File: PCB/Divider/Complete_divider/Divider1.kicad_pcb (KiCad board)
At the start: 2 copper layers, 103.8 x 48 mm, 56 parts, among them J1 10kV

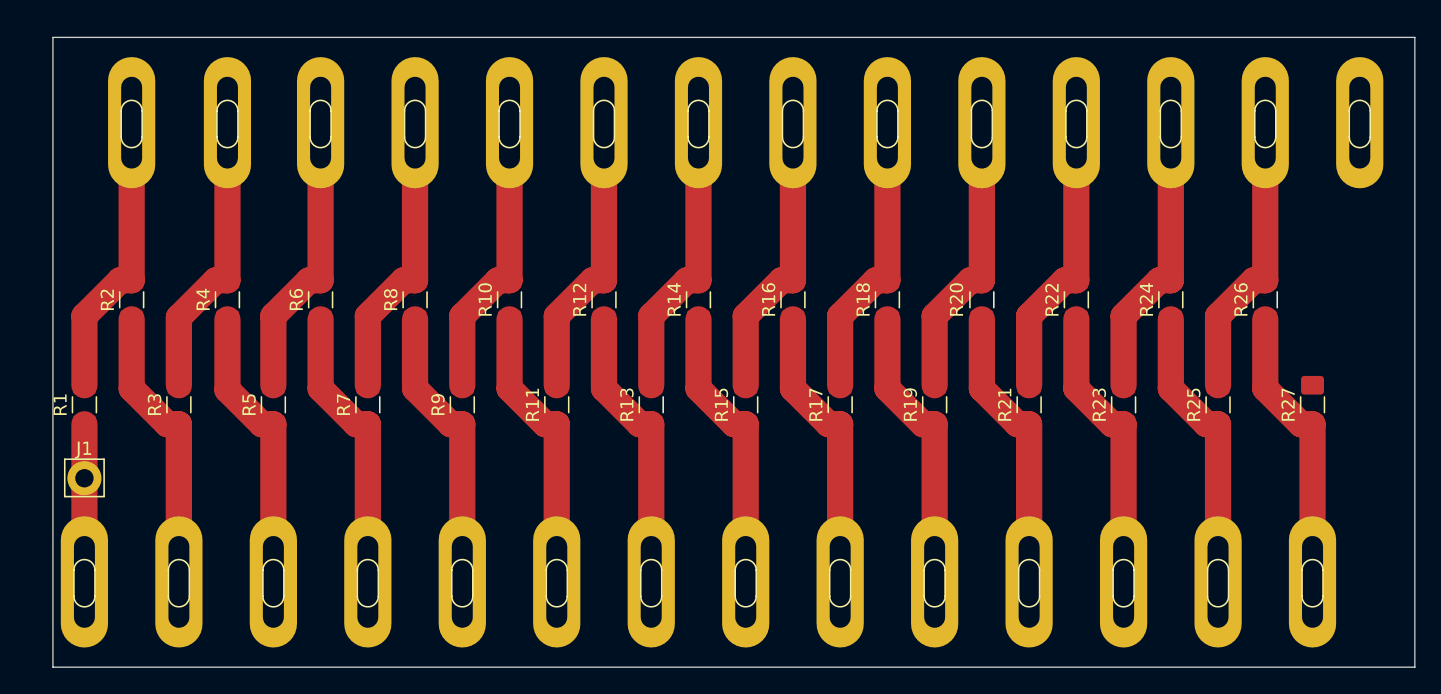
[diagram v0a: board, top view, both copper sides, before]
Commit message: Dividers finished without testing points
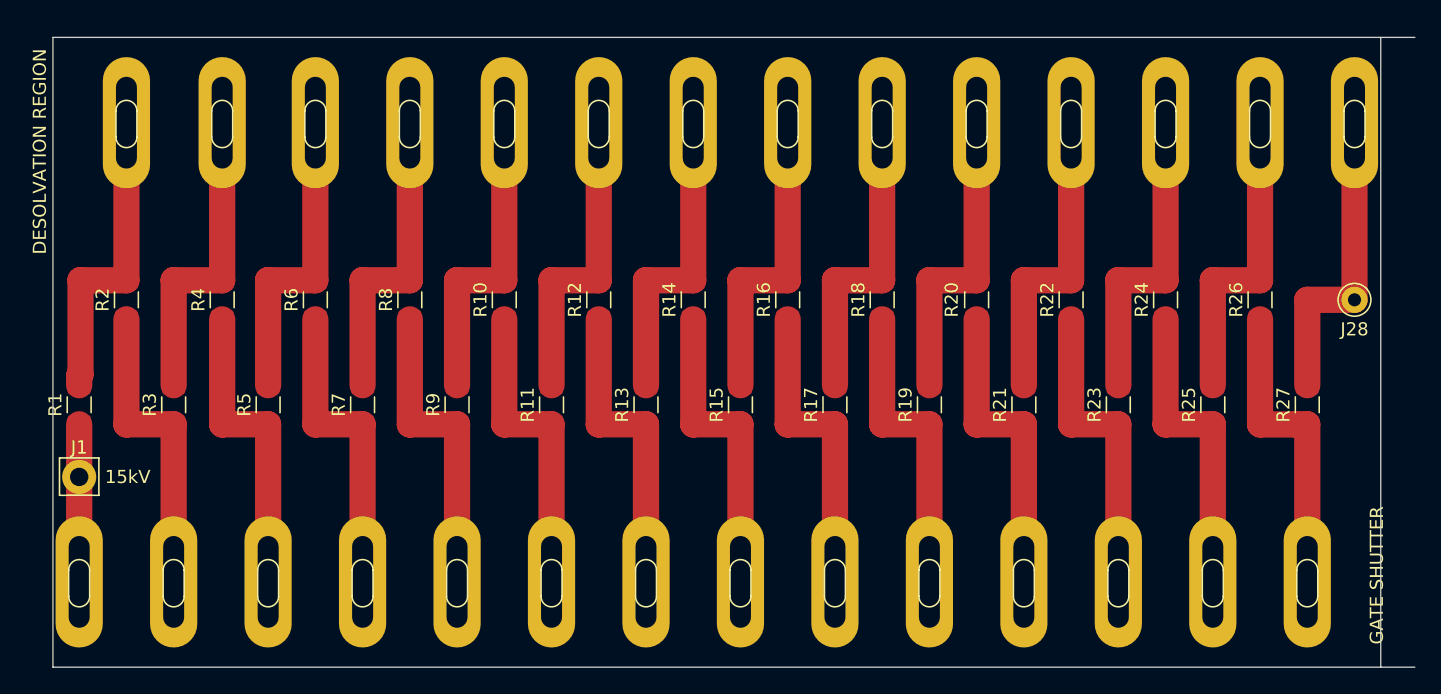
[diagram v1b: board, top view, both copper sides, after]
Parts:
- added J28: Electr., Connector_Pin:Pin_D1.0mm_L10.0mm, F.Cu at (148.2, 72.0)
- moved J1 0.41 mm to (51.0, 85.5)
- moved E11 0.40 mm to (87.0, 93.6)
- moved E12 0.40 mm to (90.6, 58.6)
- moved E14 0.40 mm to (97.8, 58.6)
- moved E16 0.40 mm to (105.0, 58.6)
- moved E17 0.40 mm to (108.6, 93.6)
- moved E19 0.40 mm to (115.8, 93.6)
- moved E21 0.40 mm to (123.0, 93.6)
- moved E22 0.40 mm to (126.6, 58.6)
- moved E23 0.40 mm to (130.2, 93.6)
- moved E25 0.40 mm to (137.4, 93.6)
- moved E26 0.40 mm to (141.0, 58.6)
- moved E27 0.40 mm to (144.6, 93.6)
- moved E28 0.40 mm to (148.2, 58.6)
- moved E6 0.40 mm to (69.0, 58.6)
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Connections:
- net DRIFTTUBE renamed DESOLVATION
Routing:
- net TRI-STATE: track 0.00 -> 23.6 mm
- net Net-(E4-Pad1): track 22.1 -> 23.7 mm
- net Net-(E24-Pad1): track 22.0 -> 23.6 mm
- net Net-(E8-Pad1): track 22.0 -> 23.6 mm
- net Net-(E20-Pad1): track 22.0 -> 23.6 mm
- net Net-(E18-Pad1): track 22.0 -> 23.6 mm
- net Net-(E15-Pad1): track 22.0 -> 23.6 mm
- net Net-(E13-Pad1): track 22.0 -> 23.6 mm
- net Net-(E10-Pad1): track 22.0 -> 23.6 mm
- net Net-(E3-Pad1): track 22.0 -> 23.6 mm
- net Net-(E27-Pad1): track 22.0 -> 23.6 mm
- net Net-(E26-Pad1): track 22.0 -> 23.6 mm
- net Net-(E7-Pad1): track 22.0 -> 23.6 mm
- net Net-(E23-Pad1): track 22.0 -> 23.6 mm
- net Net-(E22-Pad1): track 22.0 -> 23.6 mm
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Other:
- outline, holes or cut-outs redrawn
- board text added: "15kV"
- board text added: "DESOLVATION REGION"
- board text added: "GATE SHUTTER"

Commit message: Divider finished with test points
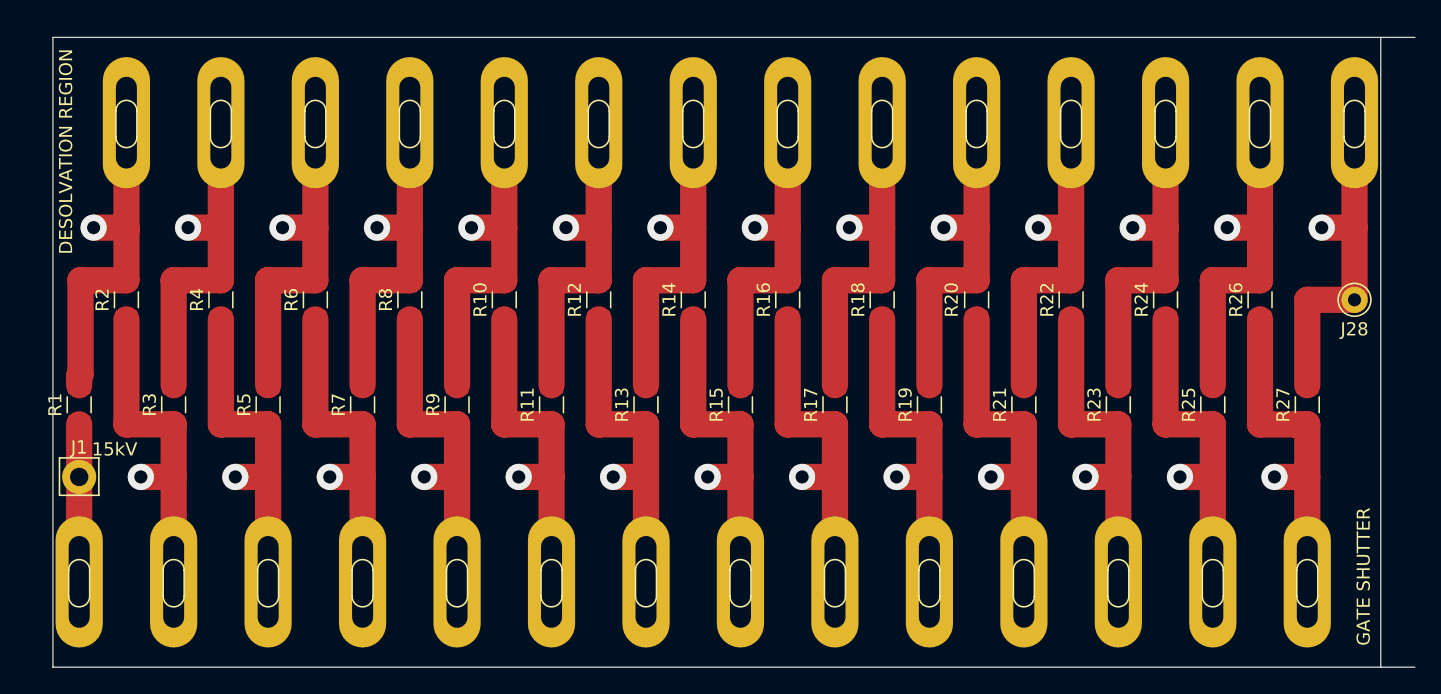
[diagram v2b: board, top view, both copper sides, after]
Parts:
- moved E4 0.10 mm to (61.8, 58.6)
- moved R4 0.10 mm to (61.8, 72.0)
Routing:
- net Net-(E5-Pad1): track 23.5 -> 26.1 mm, vias 0 -> 1
- net Net-(E24-Pad1): track 23.6 -> 26.1 mm, vias 0 -> 1
- net Net-(E2-Pad1): track 23.6 -> 26.1 mm, vias 0 -> 1
- net TRI-STATE: track 23.6 -> 26.1 mm, vias 0 -> 1
- net Net-(E9-Pad1): track 23.6 -> 26.1 mm, vias 0 -> 1
- net Net-(E8-Pad1): track 23.6 -> 26.1 mm, vias 0 -> 1
- net Net-(E7-Pad1): track 23.6 -> 26.1 mm, vias 0 -> 1
- net Net-(E6-Pad1): track 23.6 -> 26.1 mm, vias 0 -> 1
- net Net-(E3-Pad1): track 23.6 -> 26.1 mm, vias 0 -> 1
- net Net-(E27-Pad1): track 23.6 -> 26.1 mm, vias 0 -> 1
- net Net-(E26-Pad1): track 23.6 -> 26.1 mm, vias 0 -> 1
- net Net-(E25-Pad1): track 23.6 -> 26.1 mm, vias 0 -> 1
- net Net-(E22-Pad1): track 23.6 -> 26.1 mm, vias 0 -> 1
- net Net-(E21-Pad1): track 23.6 -> 26.1 mm, vias 0 -> 1
- net Net-(E20-Pad1): track 23.6 -> 26.1 mm, vias 0 -> 1
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
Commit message: Updates of dividers 1 & 2
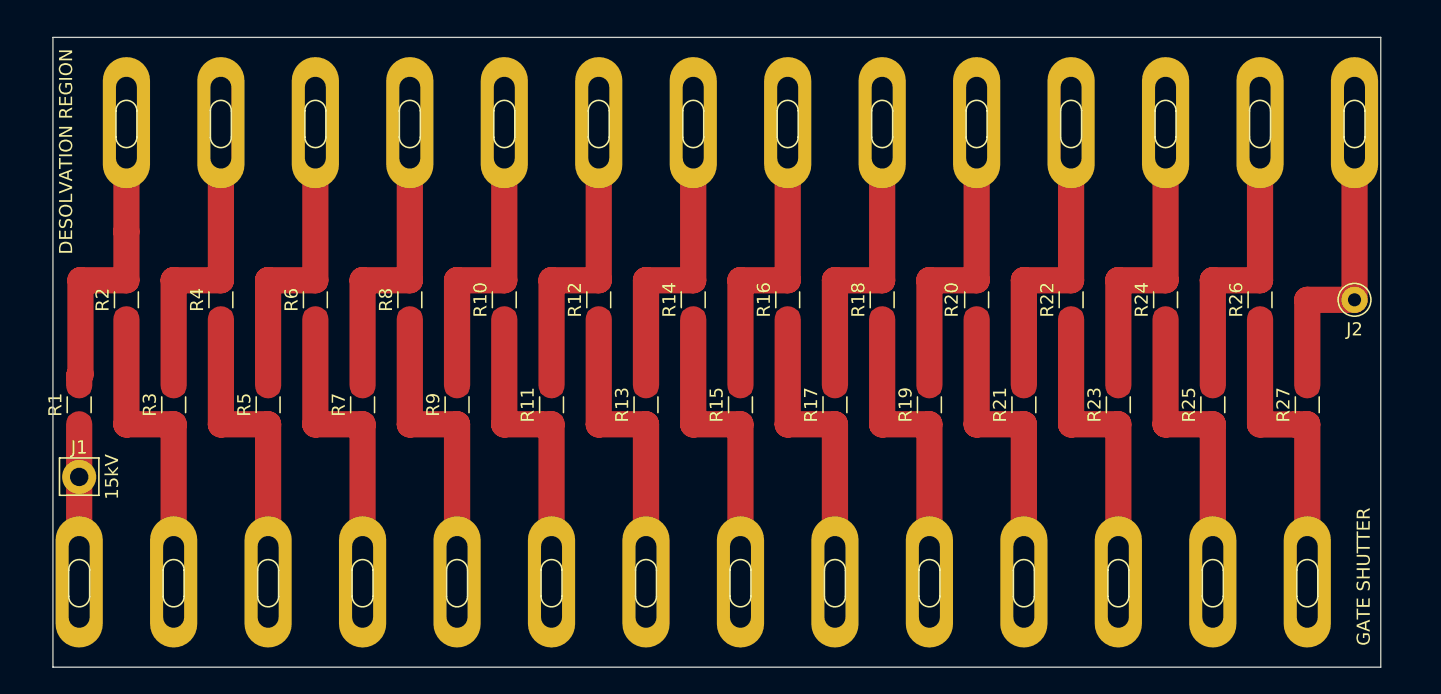
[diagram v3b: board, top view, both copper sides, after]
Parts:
- J1: value 10kV -> 15kV
- renumbered J28 to J2
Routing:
- net Net-(E5-Pad1): track 26.1 -> 23.6 mm, vias 1 -> 0
- net Net-(E24-Pad1): track 26.1 -> 23.6 mm, vias 1 -> 0
- net TRI-STATE: track 26.1 -> 23.6 mm, vias 1 -> 0
- net Net-(E9-Pad1): track 26.1 -> 23.6 mm, vias 1 -> 0
- net Net-(E8-Pad1): track 26.1 -> 23.6 mm, vias 1 -> 0
- net Net-(E7-Pad1): track 26.1 -> 23.6 mm, vias 1 -> 0
- net Net-(E6-Pad1): track 26.1 -> 23.6 mm, vias 1 -> 0
- net Net-(E4-Pad1): track 26.1 -> 23.6 mm, vias 1 -> 0
- net Net-(E3-Pad1): track 26.1 -> 23.6 mm, vias 1 -> 0
- net Net-(E27-Pad1): track 26.1 -> 23.6 mm, vias 1 -> 0
- net Net-(E26-Pad1): track 26.1 -> 23.6 mm, vias 1 -> 0
- net Net-(E25-Pad1): track 26.1 -> 23.6 mm, vias 1 -> 0
- net Net-(E22-Pad1): track 26.1 -> 23.6 mm, vias 1 -> 0
- net Net-(E21-Pad1): track 26.1 -> 23.6 mm, vias 1 -> 0
- net Net-(E20-Pad1): track 26.1 -> 23.6 mm, vias 1 -> 0
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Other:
- board size 103.8 x 48 mm -> 101.2 x 48 mm
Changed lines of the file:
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@@
     (thickness 1.6)
     (drawings 15)
-    (tracks 195)
+    (tracks 114)
     (zones 0)
     (modules 57)
@@
     (descr "solder Pin_ diameter 1.0mm, hole diameter 1.0mm (press fit), length 10.0mm")
     (tags "solder Pin_ press fit")
-    (fp_text reference J28 (at 0 2.25) (layer F.SilkS)
+    (fp_text reference J2 (at 0 2.25) (layer F.SilkS)
       (effects (font (size 1 1) (thickness 0.15)))
     )
@@
       (effects (font (size 1 1) (thickness 0.15)))
     )
-    (fp_text value 10kV (at 0 -2.05) (layer F.Fab)
+    (fp_text value 15kV (at 0 -2.05) (layer F.Fab)
       (effects (font (size 1 1) (thickness 0.15)))
     )
@@
     )
   )
+  (gr_line (start 49 100) (end 150.2 100) (layer Edge.Cuts) (width 0.05))
   (gr_text "GATE SHUTTER" (at 148.9 93.1 90) (layer F.SilkS)
     (effects (font (size 1 1) (thickness 0.15)))
@@
     (effects (font (size 1 1) (thickness 0.15)))
   )
-  (gr_text "15kV\n" (at 53.7 83.4) (layer F.SilkS)
+  (gr_text "15kV\n" (at 53.5 85.5 90) (layer F.SilkS)
     (effects (font (size 1 1) (thickness 0.15)))
   )
@@
   (gr_line (start 44.2 93.5) (end 150.6 93.5) (layer Dwgs.User) (width 0.15))
   (gr_line (start 150.2 100) (end 150.2 52) (layer Edge.Cuts) (width 0.05))
-  (gr_line (start 49 100) (end 152.8 100) (layer Edge.Cuts) (width 0.05))
   (gr_line (start 49 52) (end 49 100) (layer Edge.Cuts) (width 0.05))
   (dimension 101.2 (width 0.15) (layer Dwgs.User)
@@
     (arrow2b (pts (xy 29.434179 52.129268) (xy 30.035768 53.247745)))
   )
-  (gr_line (start 152.8 52) (end 49 52) (layer Edge.Cuts) (width 0.05))
+  (gr_line (start 150.2 52) (end 49 52) (layer Edge.Cuts) (width 0.05))
   (segment (start 51.1125 70.5125) (end 54.6 70.5125) (width 2) (layer F.Cu) (net 1))
   (segment (start 51.1 70.5) (end 51.1125 70.5125) (width 2) (layer F.Cu) (net 1))
@@
   (segment (start 54.6 70.5125) (end 54.6 66.8) (width 2) (layer F.Cu) (net 1))
   (segment (start 54.6 66.8) (end 54.6 58.5) (width 2) (layer F.Cu) (net 1))
-  (segment (start 54.6 66.5) (end 52.1 66.5) (width 2) (layer F.Cu) (net 1))
-  (segment (start 52.1 66.5) (end 52.1 66.5) (width 2) (layer F.Cu) (net 1))
-  (via (at 52.1 66.5) (size 2) (drill 1) (layers F.Cu B.Cu) (net 1))
-  (via (at 59.3 66.5) (size 2) (drill 1) (layers F.Cu B.Cu) (net 3))
-  (via (at 66.5 66.5) (size 2) (drill 1) (layers F.Cu B.Cu) (net 5))
-  (via (at 73.7 66.5) (size 2) (drill 1) (layers F.Cu B.Cu) (net 7))
-  (via (at 80.9 66.5) (size 2) (drill 1) (layers F.Cu B.Cu) (net 9))
-  (via (at 88.1 66.5) (size 2) (drill 1) (layers F.Cu B.Cu) (net 11))
-  (via (at 95.3 66.5) (size 2) (drill 1) (layers F.Cu B.Cu) (net 13))
-  (via (at 102.5 66.5) (size 2) (drill 1) (layers F.Cu B.Cu) (net 14))
-  (via (at 109.7 66.5) (size 2) (drill 1) (layers F.Cu B.Cu) (net 16))
-  (via (at 116.9 66.5) (size 2) (drill 1) (layers F.Cu B.Cu) (net 18))
-  (via (at 124.1 66.5) (size 2) (drill 1) (layers F.Cu B.Cu) (net 20))
-  (via (at 131.3 66.5) (size 2) (drill 1) (layers F.Cu B.Cu) (net 22))
-  (via (at 138.5 66.5) (size 2) (drill 1) (layers F.Cu B.Cu) (net 24))
-  (via (at 145.7 66.5) (size 2) (drill 1) (layers F.Cu B.Cu) (net 26))
-  (via (at 55.7 85.5) (size 2) (drill 1) (layers F.Cu B.Cu) (net 2))
-  (via (at 62.9 85.5) (size 2) (drill 1) (layers F.Cu B.Cu) (net 4))
-  (via (at 70.1 85.5) (size 2) (drill 1) (layers F.Cu B.Cu) (net 6))
-  (via (at 77.3 85.5) (size 2) (drill 1) (layers F.Cu B.Cu) (net 8))
-  (via (at 84.5 85.5) (size 2) (drill 1) (layers F.Cu B.Cu) (net 10))
-  (via (at 91.7 85.5) (size 2) (drill 1) (layers F.Cu B.Cu) (net 12))
-  (via (at 98.9 85.5) (size 2) (drill 1) (layers F.Cu B.Cu) (net 27))
-  (via (at 106.1 85.5) (size 2) (drill 1) (layers F.Cu B.Cu) (net 15))
-  (via (at 113.3 85.5) (size 2) (drill 1) (layers F.Cu B.Cu) (net 17))
-  (via (at 120.5 85.5) (size 2) (drill 1) (layers F.Cu B.Cu) (net 19))
-  (via (at 127.7 85.5) (size 2) (drill 1) (layers F.Cu B.Cu) (net 21))
-  (via (at 134.9 85.5) (size 2) (drill 1) (layers F.Cu B.Cu) (net 23))
-  (via (at 142.1 85.5) (size 2) (drill 1) (layers F.Cu B.Cu) (net 25))
-  (segment (start 59.3 66.5) (end 59.3 66.5) (width 2) (layer F.Cu) (net 3))
-  (segment (start 66.5 66.5) (end 66.5 66.5) (width 2) (layer F.Cu) (net 5))
-  (segment (start 73.7 66.5) (end 73.7 66.5) (width 2) (layer F.Cu) (net 7))
-  (segment (start 80.9 66.5) (end 80.9 66.5) (width 2) (layer F.Cu) (net 9))
-  (segment (start 88.1 66.5) (end 88.1 66.5) (width 2) (layer F.Cu) (net 11))
-  (segment (start 95.3 66.5) (end 95.3 66.5) (width 2) (layer F.Cu) (net 13))
-  (segment (start 102.5 66.5) (end 102.5 66.5) (width 2) (layer F.Cu) (net 14))
-  (segment (start 109.7 66.5) (end 109.7 66.5) (width 2) (layer F.Cu) (net 16))
-  (segment (start 116.9 66.5) (end 116.9 66.5) (width 2) (layer F.Cu) (net 18))
-  (segment (start 124.1 66.5) (end 124.1 66.5) (width 2) (layer F.Cu) (net 20))
-  (segment (start 131.3 66.5) (end 131.3 66.5) (width 2) (layer F.Cu) (net 22))
-  (segment (start 138.5 66.5) (end 138.5 66.5) (width 2) (layer F.Cu) (net 24))
-  (segment (start 145.7 66.5) (end 145.7 66.5) (width 2) (layer F.Cu) (net 26))
-  (segment (start 55.7 85.5) (end 55.7 85.5) (width 2) (layer F.Cu) (net 2))
-  (segment (start 62.9 85.5) (end 62.9 85.5) (width 2) (layer F.Cu) (net 4))
-  (segment (start 70.1 85.5) (end 70.1 85.5) (width 2) (layer F.Cu) (net 6))
-  (segment (start 77.3 85.5) (end 77.3 85.5) (width 2) (layer F.Cu) (net 8))
-  (segment (start 84.5 85.5) (end 84.5 85.5) (width 2) (layer F.Cu) (net 10))
-  (segment (start 91.7 85.5) (end 91.7 85.5) (width 2) (layer F.Cu) (net 12))
-  (segment (start 98.9 85.5) (end 98.9 85.5) (width 2) (layer F.Cu) (net 27))
-  (segment (start 106.1 85.5) (end 106.1 85.5) (width 2) (layer F.Cu) (net 15))
-  (segment (start 113.3 85.5) (end 113.3 85.5) (width 2) (layer F.Cu) (net 17))
-  (segment (start 120.5 85.5) (end 120.5 85.5) (width 2) (layer F.Cu) (net 19))
-  (segment (start 127.7 85.5) (end 127.7 85.5) (width 2) (layer F.Cu) (net 21))
-  (segment (start 134.9 85.5) (end 134.9 85.5) (width 2) (layer F.Cu) (net 23))
-  (segment (start 142.1 85.5) (end 142.1 85.5) (width 2) (layer F.Cu) (net 25))
-  (segment (start 61.8 66.5) (end 59.3 66.5) (width 2) (layer F.Cu) (net 3))
-  (segment (start 69 66.5) (end 66.5 66.5) (width 2) (layer F.Cu) (net 5))
-  (segment (start 76.2 66.5) (end 73.7 66.5) (width 2) (layer F.Cu) (net 7))
-  (segment (start 83.4 66.5) (end 80.9 66.5) (width 2) (layer F.Cu) (net 9))
-  (segment (start 90.6 66.5) (end 88.1 66.5) (width 2) (layer F.Cu) (net 11))
-  (segment (start 97.8 66.5) (end 95.3 66.5) (width 2) (layer F.Cu) (net 13))
-  (segment (start 105 66.5) (end 102.5 66.5) (width 2) (layer F.Cu) (net 14))
-  (segment (start 112.2 66.5) (end 109.7 66.5) (width 2) (layer F.Cu) (net 16))
-  (segment (start 119.4 66.5) (end 116.9 66.5) (width 2) (layer F.Cu) (net 18))
-  (segment (start 126.6 66.5) (end 124.1 66.5) (width 2) (layer F.Cu) (net 20))
-  (segment (start 133.8 66.5) (end 131.3 66.5) (width 2) (layer F.Cu) (net 22))
-  (segment (start 141 66.5) (end 138.5 66.5) (width 2) (layer F.Cu) (net 24))
-  (segment (start 148.2 66.5) (end 145.7 66.5) (width 2) (layer F.Cu) (net 26))
-  (segment (start 58.2 85.5) (end 55.7 85.5) (width 2) (layer F.Cu) (net 2))
-  (segment (start 65.4 85.5) (end 62.9 85.5) (width 2) (layer F.Cu) (net 4))
-  (segment (start 72.6 85.5) (end 70.1 85.5) (width 2) (layer F.Cu) (net 6))
-  (segment (start 79.8 85.5) (end 77.3 85.5) (width 2) (layer F.Cu) (net 8))
-  (segment (start 87 85.5) (end 84.5 85.5) (width 2) (layer F.Cu) (net 10))
-  (segment (start 94.2 85.5) (end 91.7 85.5) (width 2) (layer F.Cu) (net 12))
-  (segment (start 101.4 85.5) (end 98.9 85.5) (width 2) (layer F.Cu) (net 27))
-  (segment (start 108.6 85.5) (end 106.1 85.5) (width 2) (layer F.Cu) (net 15))
-  (segment (start 115.8 85.5) (end 113.3 85.5) (width 2) (layer F.Cu) (net 17))
-  (segment (start 123 85.5) (end 120.5 85.5) (width 2) (layer F.Cu) (net 19))
-  (segment (start 130.2 85.5) (end 127.7 85.5) (width 2) (layer F.Cu) (net 21))
-  (segment (start 137.4 85.5) (end 134.9 85.5) (width 2) (layer F.Cu) (net 23))
-  (segment (start 144.6 85.5) (end 142.1 85.5) (width 2) (layer F.Cu) (net 25))
   (segment (start 58.2 81.4875) (end 58.2 93.5) (width 2) (layer F.Cu) (net 2))
   (segment (start 54.6 73.4875) (end 54.6 81.5) (width 2) (layer F.Cu) (net 2))
